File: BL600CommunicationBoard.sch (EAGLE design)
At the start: 29 parts, among them IC1 MAX3218, IC2 LM2937ET, IC3 MAX3218, X1 RS-232

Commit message: Added com board layout
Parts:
- removed R2, R5, R6: 0, rcl:R-EU_0207/10
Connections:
- removed net N$14: IC1.T1IN, R5.2
- removed net N$15: IC1.T2IN, R6.2
- removed net N$6: IC3.R2OUT, SV4.8
- net GND: now also IC1.R2IN, IC1.T1IN, IC1.T2IN, SV4.9; no longer R2.2, R5.1, R6.1
- net N$2: now also IC3.T2IN, SV4.8; no longer IC1.R2IN, R2.1
- net N$3: now also SV4.4; no longer SV4.2
- net N$4: now also IC3.R1OUT, SV4.2; no longer IC3.T2IN, SV4.4
- net N$5: now also IC3.R2OUT; no longer IC3.R1OUT
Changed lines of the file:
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@@
 <part name="GND9" library="supply1" deviceset="GND" device=""/>
 <part name="GND10" library="supply1" deviceset="GND" device=""/>
-<part name="R5" library="rcl" deviceset="R-EU_" device="0207/10" value="0"/>
-<part name="R6" library="rcl" deviceset="R-EU_" device="0207/10" value="0"/>
 <part name="GND11" library="supply1" deviceset="GND" device=""/>
 <part name="GND12" library="supply1" deviceset="GND" device=""/>
@@
 <part name="GND15" library="supply1" deviceset="GND" device=""/>
 <part name="GND16" library="supply1" deviceset="GND" device=""/>
-<part name="R2" library="rcl" deviceset="R-EU_" device="0207/10" value="0"/>
 <part name="GND7" library="supply1" deviceset="GND" device=""/>
+<part name="GND17" library="supply1" deviceset="GND" device=""/>
 </parts>
 <sheets>
@@
 <instance part="GND9" gate="1" x="218.44" y="38.1"/>
 <instance part="GND10" gate="1" x="165.1" y="-2.54"/>
-<instance part="R5" gate="G$1" x="127" y="-35.56"/>
-<instance part="R6" gate="G$1" x="127" y="-43.18"/>
 <instance part="GND11" gate="1" x="124.46" y="-22.86"/>
 <instance part="GND12" gate="1" x="185.42" y="-22.86"/>
 <instance part="GND13" gate="1" x="193.04" y="-38.1"/>
-<instance part="GND14" gate="1" x="119.38" y="-35.56" rot="R270"/>
-<instance part="GND15" gate="1" x="119.38" y="-43.18" rot="R270"/>
+<instance part="GND14" gate="1" x="129.54" y="-35.56" rot="R270"/>
+<instance part="GND15" gate="1" x="129.54" y="-43.18" rot="R270"/>
 <instance part="GND16" gate="1" x="165.1" y="-78.74"/>
-<instance part="R2" gate="G$1" x="182.88" y="-58.42"/>
-<instance part="GND7" gate="1" x="190.5" y="-58.42" rot="R90"/>
+<instance part="GND7" gate="1" x="180.34" y="-58.42" rot="R90"/>
+<instance part="GND17" gate="1" x="88.9" y="12.7"/>
 </instances>
 <busses>
@@
 </segment>
 <segment>
-<pinref part="R5" gate="G$1" pin="1"/>
-<pinref part="GND14" gate="1" pin="GND"/>
-</segment>
-<segment>
-<pinref part="R6" gate="G$1" pin="1"/>
-<pinref part="GND15" gate="1" pin="GND"/>
-</segment>
-<segment>
 <pinref part="IC1" gate="G$1" pin="GND3"/>
 <pinref part="GND16" gate="1" pin="GND"/>
@@
 </segment>
 <segment>
-<pinref part="R2" gate="G$1" pin="2"/>
+<pinref part="IC1" gate="G$1" pin="T1IN"/>
+<pinref part="GND14" gate="1" pin="GND"/>
+</segment>
+<segment>
+<pinref part="IC1" gate="G$1" pin="T2IN"/>
+<pinref part="GND15" gate="1" pin="GND"/>
+</segment>
+<segment>
+<pinref part="IC1" gate="G$1" pin="R2IN"/>
 <pinref part="GND7" gate="1" pin="GND"/>
+</segment>
+<segment>
+<pinref part="SV4" gate="G$1" pin="9"/>
+<pinref part="GND17" gate="1" pin="GND"/>
 </segment>
 </net>
@@
 </segment>
 </net>
-<net name="N$3" class="0">
-<segment>
-<pinref part="SV4" gate="G$1" pin="2"/>
-<wire x1="104.14" y1="25.4" x2="116.84" y2="25.4" width="0.1524" layer="91"/>
-<wire x1="116.84" y1="25.4" x2="116.84" y2="40.64" width="0.1524" layer="91"/>
-<pinref part="IC3" gate="G$1" pin="T1IN"/>
-<wire x1="116.84" y1="40.64" x2="132.08" y2="40.64" width="0.1524" layer="91"/>
-</segment>
-</net>
-<net name="N$4" class="0">
-<segment>
-<pinref part="SV4" gate="G$1" pin="4"/>
-<wire x1="104.14" y1="22.86" x2="119.38" y2="22.86" width="0.1524" layer="91"/>
-<wire x1="119.38" y1="22.86" x2="119.38" y2="33.02" width="0.1524" layer="91"/>
-<pinref part="IC3" gate="G$1" pin="T2IN"/>
-<wire x1="119.38" y1="33.02" x2="132.08" y2="33.02" width="0.1524" layer="91"/>
-</segment>
-</net>
 <net name="N$5" class="0">
 <segment>
 <pinref part="SV4" gate="G$1" pin="6"/>
 <wire x1="104.14" y1="20.32" x2="121.92" y2="20.32" width="0.1524" layer="91"/>
-<wire x1="121.92" y1="20.32" x2="121.92" y2="25.4" width="0.1524" layer="91"/>
-<pinref part="IC3" gate="G$1" pin="R1OUT"/>
-<wire x1="121.92" y1="25.4" x2="132.08" y2="25.4" width="0.1524" layer="91"/>
-</segment>
-</net>
-<net name="N$6" class="0">
-<segment>
-<pinref part="SV4" gate="G$1" pin="8"/>
+<wire x1="121.92" y1="20.32" x2="121.92" y2="17.78" width="0.1524" layer="91"/>
 <pinref part="IC3" gate="G$1" pin="R2OUT"/>
-<wire x1="104.14" y1="17.78" x2="132.08" y2="17.78" width="0.1524" layer="91"/>
+<wire x1="121.92" y1="17.78" x2="132.08" y2="17.78" width="0.1524" layer="91"/>
 </segment>
 </net>
@@
 <wire x1="177.8" y1="45.72" x2="185.42" y2="45.72" width="0.1524" layer="91"/>
 <wire x1="185.42" y1="45.72" x2="185.42" y2="43.18" width="0.1524" layer="91"/>
-</segment>
-</net>
-<net name="N$14" class="0">
-<segment>
-<pinref part="IC1" gate="G$1" pin="T1IN"/>
-<pinref part="R5" gate="G$1" pin="2"/>
-</segment>
-</net>
-<net name="N$15" class="0">
-<segment>
-<pinref part="IC1" gate="G$1" pin="T2IN"/>
-<pinref part="R6" gate="G$1" pin="2"/>
 </segment>
 </net>
@@
 <net name="N$2" class="0">
 <segment>
-<pinref part="IC1" gate="G$1" pin="R2IN"/>
-<pinref part="R2" gate="G$1" pin="1"/>
-</segment>
-</net>
+<pinref part="SV4" gate="G$1" pin="8"/>
+<wire x1="104.14" y1="17.78" x2="119.38" y2="17.78" width="0.1524" layer="91"/>
+<wire x1="119.38" y1="17.78" x2="119.38" y2="33.02" width="0.1524" layer="91"/>
+<pinref part="IC3" gate="G$1" pin="T2IN"/>
+<wire x1="119.38" y1="33.02" x2="132.08" y2="33.02" width="0.1524" layer="91"/>
+</segment>
+</net>
+<net name="N$3" class="0">
+<segment>
+<pinref part="SV4" gate="G$1" pin="4"/>
+<wire x1="104.14" y1="22.86" x2="116.84" y2="22.86" width="0.1524" layer="91"/>
+<wire x1="116.84" y1="22.86" x2="116.84" y2="40.64" width="0.1524" layer="91"/>
+<pinref part="IC3" gate="G$1" pin="T1IN"/>
+<wire x1="116.84" y1="40.64" x2="132.08" y2="40.64" width="0.1524" layer="91"/>
+</segment>
+</net>
+<net name="N$4" class="0">
+<segment>
+<pinref part="SV4" gate="G$1" pin="2"/>
+<pinref part="IC3" gate="G$1" pin="R1OUT"/>
+<wire x1="104.14" y1="25.4" x2="132.08" y2="25.4" width="0.1524" layer="91"/>
+</segment>
+</net>

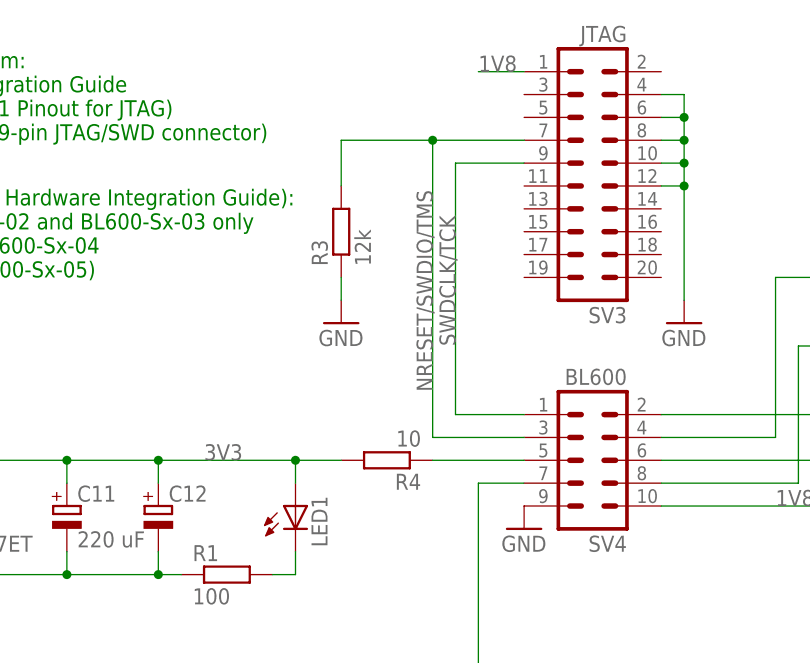
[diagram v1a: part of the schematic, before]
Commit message: Change placement of header pin for communication board, and changed to vector text in windVane layout
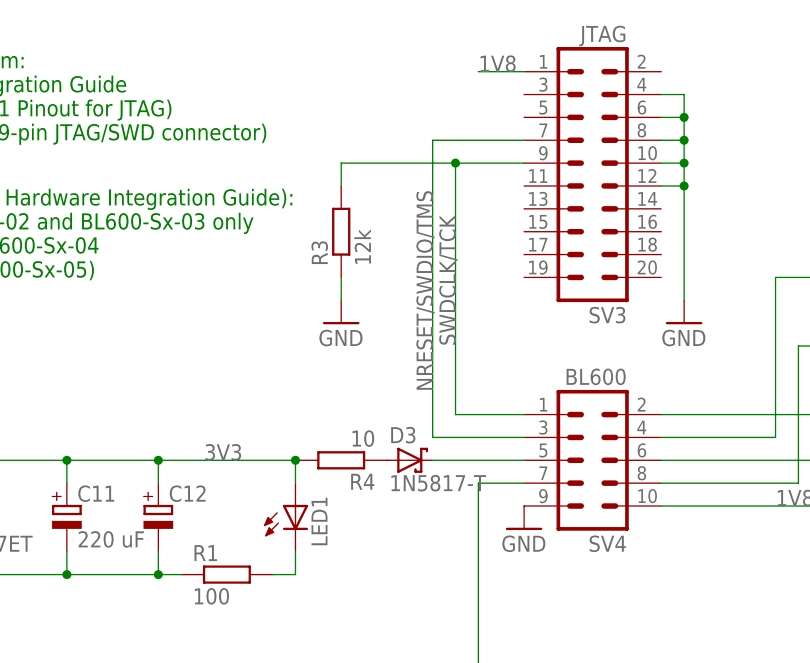
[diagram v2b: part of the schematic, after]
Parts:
- added D3: 1N5817-T, diode:1N5817-T
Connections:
- removed net N$17: R4.1, SV4.5
- new net N$6: D3.A, R4.1
- new net N$7: D3.C, SV4.5
- net NRESET/SWDIO/TMS: no longer R3.2
- net SWDCLK/TCK: now also R3.2
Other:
- moved on the sheet: R4
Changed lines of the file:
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@@
 <part name="GND7" library="supply1" deviceset="GND" device=""/>
 <part name="GND17" library="supply1" deviceset="GND" device=""/>
+<part name="D3" library="diode" deviceset="1N581*" device="" technology="7-T"/>
 </parts>
 <sheets>
@@
 <instance part="GND5" gate="1" x="208.28" y="2.54"/>
 <instance part="C12" gate="G$1" x="48.26" y="15.24"/>
-<instance part="R4" gate="G$1" x="73.66" y="20.32" rot="R180"/>
+<instance part="R4" gate="G$1" x="68.58" y="20.32" rot="R180"/>
 <instance part="IC3" gate="G$1" x="154.94" y="30.48"/>
 <instance part="IC1" gate="G$1" x="154.94" y="-45.72"/>
@@
 <instance part="GND7" gate="1" x="180.34" y="-58.42" rot="R90"/>
 <instance part="GND17" gate="1" x="88.9" y="12.7"/>
+<instance part="D3" gate="G$1" x="76.2" y="20.32"/>
 </instances>
 <busses>
@@
 <pinref part="SV4" gate="G$1" pin="3"/>
 <label x="78.74" y="27.94" size="1.778" layer="95" rot="R90"/>
-<pinref part="R3" gate="G$1" pin="2"/>
-<wire x1="68.58" y1="55.88" x2="68.58" y2="50.8" width="0.1524" layer="91"/>
-<wire x1="68.58" y1="55.88" x2="78.74" y2="55.88" width="0.1524" layer="91"/>
-<junction x="78.74" y="55.88"/>
 </segment>
 </net>
@@
 <pinref part="SV4" gate="G$1" pin="1"/>
 <label x="81.28" y="33.02" size="1.778" layer="95" rot="R90"/>
+<pinref part="R3" gate="G$1" pin="2"/>
+<wire x1="68.58" y1="50.8" x2="68.58" y2="53.34" width="0.1524" layer="91"/>
+<wire x1="68.58" y1="53.34" x2="81.28" y2="53.34" width="0.1524" layer="91"/>
+<junction x="81.28" y="53.34"/>
 </segment>
 </net>
@@
 </segment>
 </net>
-<net name="N$17" class="0">
-<segment>
-<pinref part="R4" gate="G$1" pin="1"/>
-<wire x1="78.74" y1="20.32" x2="88.9" y2="20.32" width="0.1524" layer="91"/>
-<pinref part="SV4" gate="G$1" pin="5"/>
-</segment>
-</net>
 <net name="DTR" class="0">
 <segment>
@@
 <segment>
 <pinref part="IC2" gate="1" pin="OUT"/>
-<wire x1="68.58" y1="20.32" x2="63.5" y2="20.32" width="0.1524" layer="91"/>
 <wire x1="63.5" y1="20.32" x2="48.26" y2="20.32" width="0.1524" layer="91"/>
 <wire x1="48.26" y1="20.32" x2="38.1" y2="20.32" width="0.1524" layer="91"/>
@@
 </segment>
 </net>
+<net name="N$6" class="0">
+<segment>
+<pinref part="R4" gate="G$1" pin="1"/>
+<pinref part="D3" gate="G$1" pin="A"/>
+</segment>
+</net>
+<net name="N$7" class="0">
+<segment>
+<pinref part="D3" gate="G$1" pin="C"/>
+<pinref part="SV4" gate="G$1" pin="5"/>
+<wire x1="78.74" y1="20.32" x2="88.9" y2="20.32" width="0.1524" layer="91"/>
+</segment>
+</net>
